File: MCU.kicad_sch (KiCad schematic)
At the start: 4 parts, among them IC2 PIC16F15345T-E_SSVAO, J4 Conn_ARM_SWD_TagConnect_TC203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

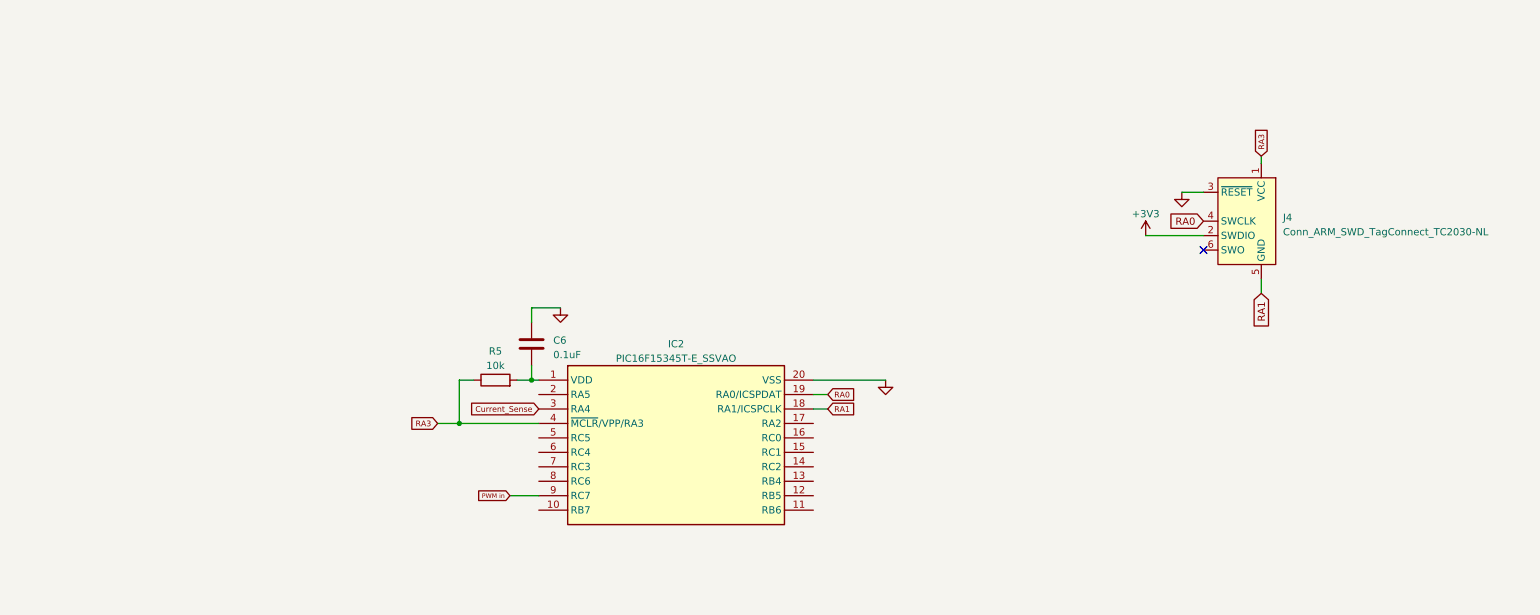
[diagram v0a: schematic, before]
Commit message: face to face switches design
with no MOVs and all other present
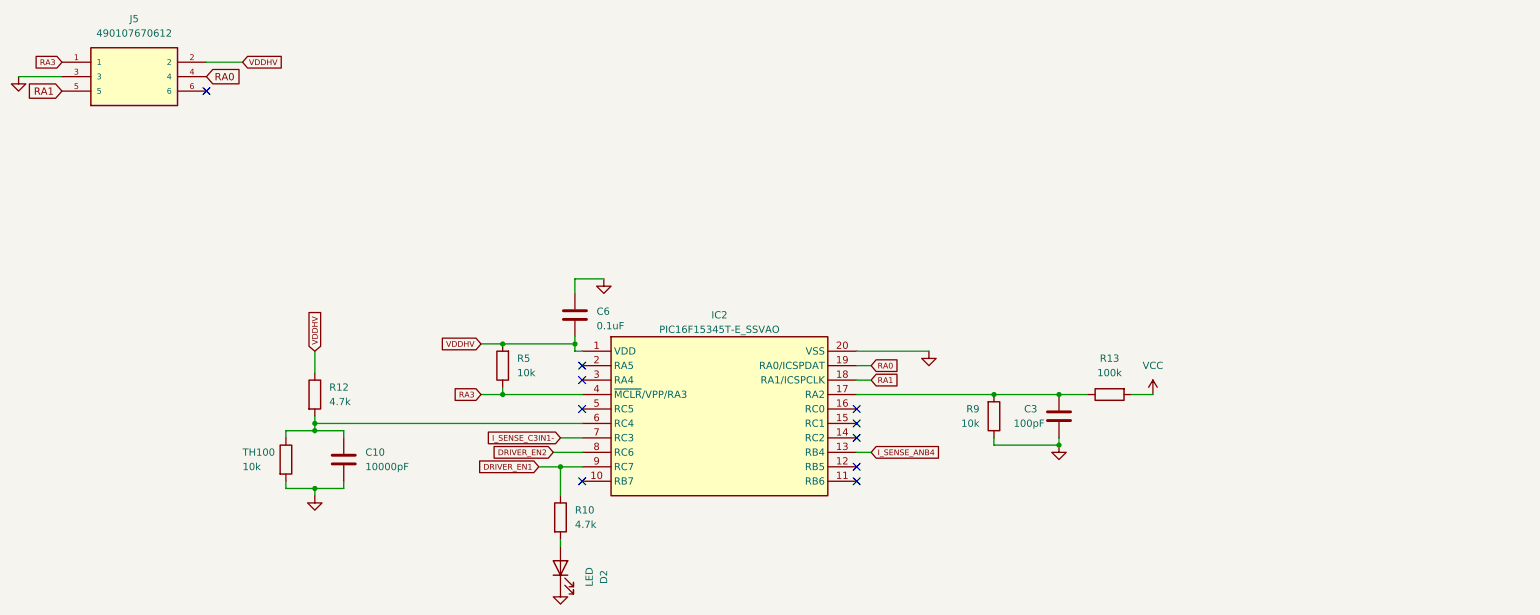
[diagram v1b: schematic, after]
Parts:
- removed J4: Conn_ARM_SWD_TagConnect_TC2030-NL, Connector:Tag-Connect_TC2030-IDC-NL_2x03_P1.27mm_Vertical, symbol Connector:Conn_ARM_SWD_TagConnect_TC2030-NL
- added C10: 10000pF, Capacitor_SMD:C_0805_2012Metric, symbol Device:C
- added C3: 100pF, Capacitor_SMD:C_0805_2012Metric, symbol Device:C
- added D2: LED, LED_SMD:LED_0805_2012Metric, symbol Device:LED
- added J5: 490107670612, 490107670612:WURTH_490107670612, symbol 490107670612:490107670612
- added R10, R12: 4.7k, Resistor_SMD:R_0805_2012Metric, symbol Device:R
- added R13: 100k, Resistor_SMD:R_0805_2012Metric, symbol Device:R
- added R9: 10k, Resistor_SMD:R_0805_2012Metric, symbol Device:R
- added TH100: 10k, Capacitor_SMD:C_0603_1608Metric, symbol Device:R
- C6: footprint (none) -> Capacitor_SMD:C_0805_2012Metric
- IC2: footprint SOP65P780X200-20N -> PIC16F15345T-E_SSVAO:SOP65P780X200-20N
- R5: footprint (none) -> Resistor_SMD:R_0805_2012Metric
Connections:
- net GND: now also C10.2, C3.2, D2.1 (K), J5.3, R9.1, TH100.2
- net RA0: now also J5.4
- net RA1: now also J5.5
- net RA3: now also J5.1
- net VDDHV: now reaches C6.2, IC2.1 (VDD), R5.2
- net VDDHV: now also J5.2, R12.1
- net I_SENSE_ANB4: now reaches IC2.13 (RB4)
- net at IC2.17 (RA2): now also C3.1, R13.1, R9.2
- net at IC2.6 (RC4): now also C10.1, R12.2, TH100.1
- net I_SENSE_C3IN1-: now reaches IC2.7 (RC3)
- net DRIVER_EN2: now reaches IC2.8 (RC6)
- net Current_Sense: no longer names the net of IC2.3 (RA4)
- net PWM in renamed DRIVER_EN1
- net DRIVER_EN1: now also R10.1
- new net: D2.2 (A), R10.2
- new net VCC: R13.2
- no-connect marks 1 -> 10
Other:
- moved on the sheet: C6, IC2, R5

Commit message: updated the design
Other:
- moved on the sheet: J5
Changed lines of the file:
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@@
   (no_connect (at 120.65 90.17))
   (no_connect (at 120.65 102.87))
-  (no_connect (at 54.61 34.29))
+  (no_connect (at 156.21 50.8))
   (no_connect (at 120.65 82.55))
   (no_connect (at 168.91 90.17))
@@
     (stroke (width 0) (type default))
   )
-  (wire (pts (xy 21.59 31.75) (xy 29.21 31.75))
+  (wire (pts (xy 123.19 48.26) (xy 130.81 48.26))
     (stroke (width 0) (type default))
   )
@@
     (stroke (width 0) (type default))
   )
-  (wire (pts (xy 60.96 29.21) (xy 54.61 29.21))
+  (wire (pts (xy 162.56 45.72) (xy 156.21 45.72))
     (stroke (width 0) (type default))
   )
@@
     )
   )
-  (global_label "RA1" (shape input) (at 29.21 34.29 180) (fields_autoplaced)
+  (global_label "RA1" (shape input) (at 130.81 50.8 180) (fields_autoplaced)
     (effects (font (size 1.27 1.27)) (justify right))
-    (property "Intersheetrefs" "${INTERSHEET_REFS}" (at 22.6567 34.29 0)
+    (property "Intersheetrefs" "${INTERSHEET_REFS}" (at 124.2567 50.8 0)
       (effects (font (size 1.27 1.27)) (justify right) hide)
     )
@@
     )
   )
-  (global_label "RA3" (shape input) (at 29.21 29.21 180) (fields_autoplaced)
-    (effects (font (size 1 1)) (justify right))
-    (property "Intersheetrefs" "${INTERSHEET_REFS}" (at 24.0502 29.21 0)
+  (global_label "RA3" (shape input) (at 130.81 45.72 180) (fields_autoplaced)
+    (effects (font (size 1 1)) (justify right))
+    (property "Intersheetrefs" "${INTERSHEET_REFS}" (at 125.6502 45.72 0)
       (effects (font (size 1.27 1.27)) (justify right) hide)
     )
@@
     )
   )
-  (global_label "VDDHV" (shape input) (at 60.96 29.21 0) (fields_autoplaced)
-    (effects (font (size 1 1)) (justify left))
-    (property "Intersheetrefs" "${INTERSHEET_REFS}" (at 68.0721 29.21 0)
+  (global_label "VDDHV" (shape input) (at 162.56 45.72 0) (fields_autoplaced)
+    (effects (font (size 1 1)) (justify left))
+    (property "Intersheetrefs" "${INTERSHEET_REFS}" (at 169.6721 45.72 0)
       (effects (font (size 1.27 1.27)) (justify left) hide)
     )
@@
     )
   )
-  (global_label "RA0" (shape input) (at 54.61 31.75 0) (fields_autoplaced)
+  (global_label "RA0" (shape input) (at 156.21 48.26 0) (fields_autoplaced)
     (effects (font (size 1.27 1.27)) (justify left))
-    (property "Intersheetrefs" "${INTERSHEET_REFS}" (at 61.1633 31.75 0)
+    (property "Intersheetrefs" "${INTERSHEET_REFS}" (at 162.7633 48.26 0)
       (effects (font (size 1.27 1.27)) (justify left) hide)
     )
@@
     )
   )
-  (symbol (lib_id "490107670612:490107670612") (at 41.91 31.75 0) (unit 1)
-    (in_bom yes) (on_board yes) (dnp no) (fields_autoplaced)
-    (property "Reference" "J5" (at 41.91 21.59 0)
+  (symbol (lib_id "490107670612:490107670612") (at 143.51 48.26 0) (unit 1)
+    (in_bom yes) (on_board yes) (dnp no) (fields_autoplaced)
+    (property "Reference" "J5" (at 143.51 38.1 0)
       (effects (font (size 1.27 1.27)))
     )
-    (property "Value" "490107670612" (at 41.91 24.13 0)
+    (property "Value" "490107670612" (at 143.51 40.64 0)
       (effects (font (size 1.27 1.27)))
     )
-    (property "Footprint" "490107670612:WURTH_490107670612" (at 41.91 31.75 0)
-      (effects (font (size 1.27 1.27)) (justify bottom) hide)
-    )
-    (property "Datasheet" "" (at 41.91 31.75 0)
-      (effects (font (size 1.27 1.27)) hide)
-    )
-    (property "PARTREV" "002.003" (at 41.91 31.75 0)
-      (effects (font (size 1.27 1.27)) (justify bottom) hide)
-    )
-    (property "STANDARD" "Manufacturer Recommendations" (at 41.91 31.75 0)
-      (effects (font (size 1.27 1.27)) (justify bottom) hide)
-    )
-    (property "MAXIMUM_PACKAGE_HEIGHT" "10.45 mm" (at 41.91 31.75 0)
-      (effects (font (size 1.27 1.27)) (justify bottom) hide)
-    )
-    (property "MANUFACTURER" "Würth Elektronik" (at 41.91 31.75 0)
+    (property "Footprint" "490107670612:WURTH_490107670612" (at 143.51 48.26 0)
+      (effects (font (size 1.27 1.27)) (justify bottom) hide)
+    )
+    (property "Datasheet" "" (at 143.51 48.26 0)
+      (effects (font (size 1.27 1.27)) hide)
+    )
+    (property "PARTREV" "002.003" (at 143.51 48.26 0)
+      (effects (font (size 1.27 1.27)) (justify bottom) hide)
+    )
+    (property "STANDARD" "Manufacturer Recommendations" (at 143.51 48.26 0)
+      (effects (font (size 1.27 1.27)) (justify bottom) hide)
+    )
+    (property "MAXIMUM_PACKAGE_HEIGHT" "10.45 mm" (at 143.51 48.26 0)
+      (effects (font (size 1.27 1.27)) (justify bottom) hide)
+    )
+    (property "MANUFACTURER" "Würth Elektronik" (at 143.51 48.26 0)
       (effects (font (size 1.27 1.27)) (justify bottom) hide)
     )
@@
     )
   )
-  (symbol (lib_id "power:GND") (at 21.59 31.75 0) (unit 1)
-    (in_bom yes) (on_board yes) (dnp no) (fields_autoplaced)
-    (property "Reference" "#PWR01" (at 21.59 38.1 0)
-      (effects (font (size 1.27 1.27)) hide)
-    )
-    (property "Value" "GND" (at 21.59 36.83 0)
-      (effects (font (size 1.27 1.27)) hide)
-    )
-    (property "Footprint" "" (at 21.59 31.75 0)
-      (effects (font (size 1.27 1.27)) hide)
-    )
-    (property "Datasheet" "" (at 21.59 31.75 0)
-      (effects (font (size 1.27 1.27)) hide)
-    )
+  (symbol (lib_id "power:GND") (at 123.19 48.26 0) (unit 1)
+    (in_bom yes) (on_board yes) (dnp no) (fields_autoplaced)
+    (property "Reference" "#PWR01" (at 123.19 54.61 0)
+      (effects (font (size 1.27 1.27)) hide)
+    )
+    (property "Value" "GND" (at 123.19 53.34 0)
+      (effects (font (size 1.27 1.27)) hide)
+    )
+    (property "Footprint" "" (at 123.19 48.26 0)
+      (effects (font (size 1.27 1.27)) hide)
+    )
+    (property "Datasheet" "" (at 123.19 48.26 0)
+      (effects (font (size 1.27 1.27)) hide)
+    )

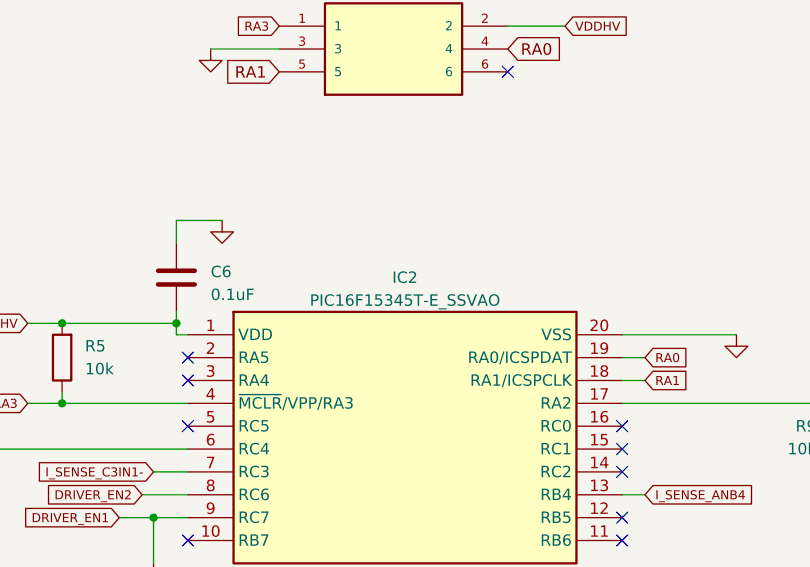
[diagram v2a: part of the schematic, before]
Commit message: Design with footprint error
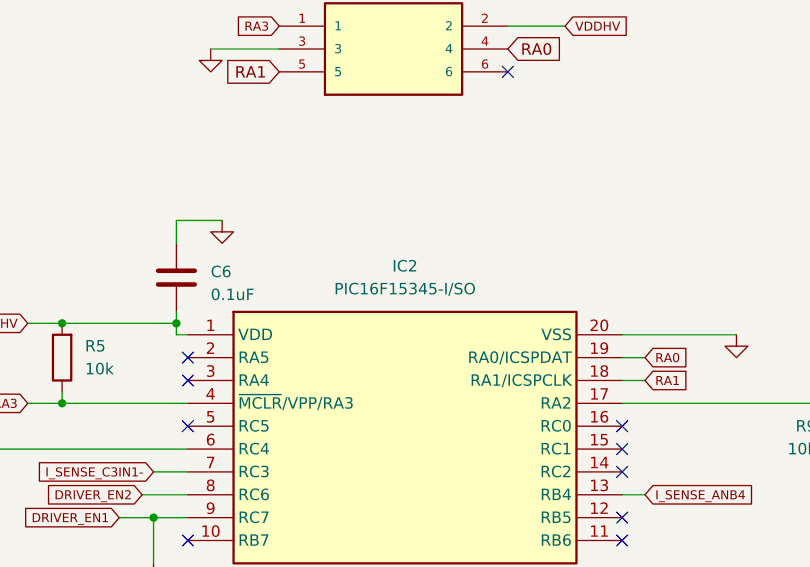
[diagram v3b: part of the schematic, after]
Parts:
- IC2: value PIC16F15345T-E_SSVAO -> PIC16F15345-I/SO; footprint PIC16F15345T-E_SSVAO:SOP65P780X200-20N -> PIC16F15345-ISO:SOIC127P1030X265-20N
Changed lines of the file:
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@@
   (symbol (lib_id "PIC16F15345T-E_SSVAO:PIC16F15345T-E_SSVAO") (at 120.65 80.01 0) (unit 1)
     (in_bom yes) (on_board yes) (dnp no) (fields_autoplaced)
-    (property "Reference" "IC2" (at 144.78 73.66 0)
+    (property "Reference" "IC2" (at 144.78 72.39 0)
       (effects (font (size 1.27 1.27)))
     )
-    (property "Value" "PIC16F15345T-E_SSVAO" (at 144.78 76.2 0)
+    (property "Value" "PIC16F15345-I/SO" (at 144.78 74.93 0)
       (effects (font (size 1.27 1.27)))
     )
-    (property "Footprint" "PIC16F15345T-E_SSVAO:SOP65P780X200-20N" (at 165.1 174.93 0)
+    (property "Footprint" "PIC16F15345-ISO:SOIC127P1030X265-20N" (at 165.1 174.93 0)
       (effects (font (size 1.27 1.27)) (justify left top) hide)
     )

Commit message: Final Design
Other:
- moved on the sheet: C10, C3, J5, R12, R13, R5, R9, TH100
